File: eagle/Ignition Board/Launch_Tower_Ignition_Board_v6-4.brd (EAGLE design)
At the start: 87.6 x 69.8 mm, 41 parts, among them IC1 INVERT GATES, IC2 OPTOISOLATOR, Q1 NMOSFET, U1 SN65220DBV

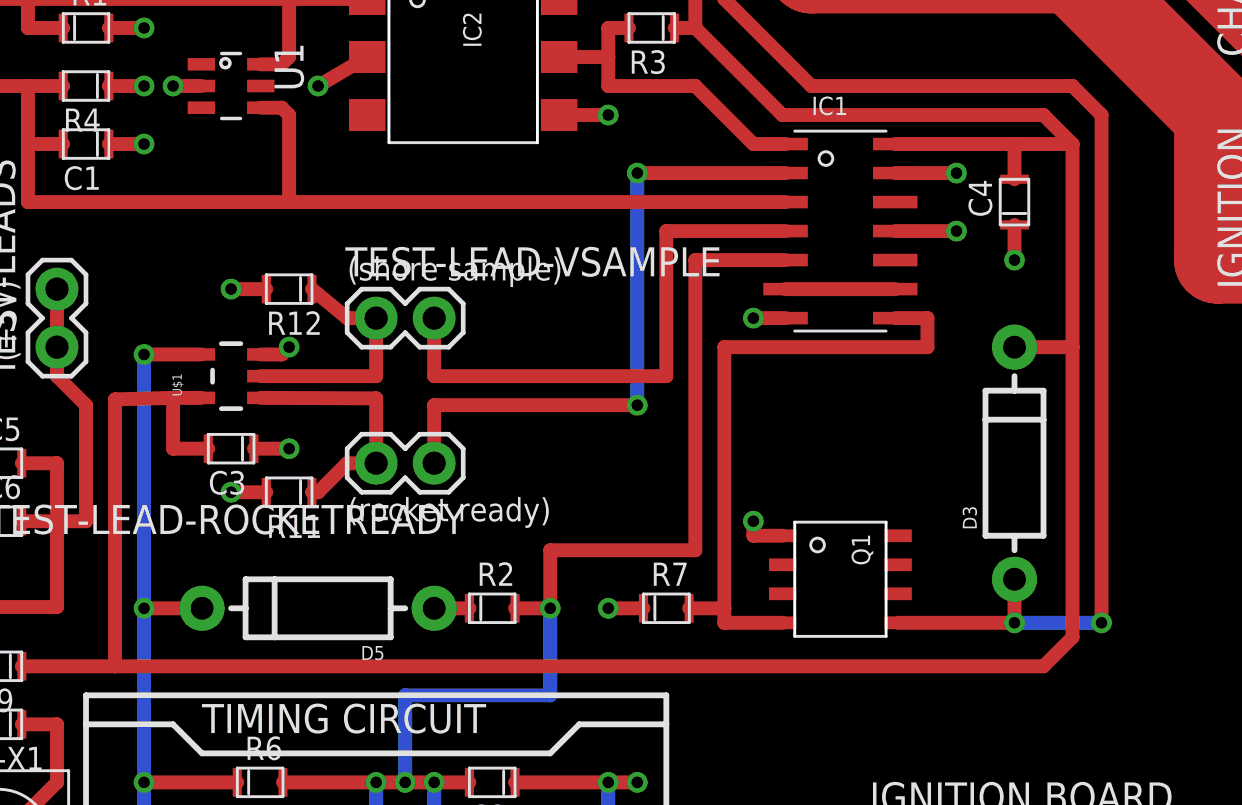
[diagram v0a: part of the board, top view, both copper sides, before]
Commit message: Minor changes to Ignition board and library - smaller diode Signed-off-by: richard <richard@mailwh.com>
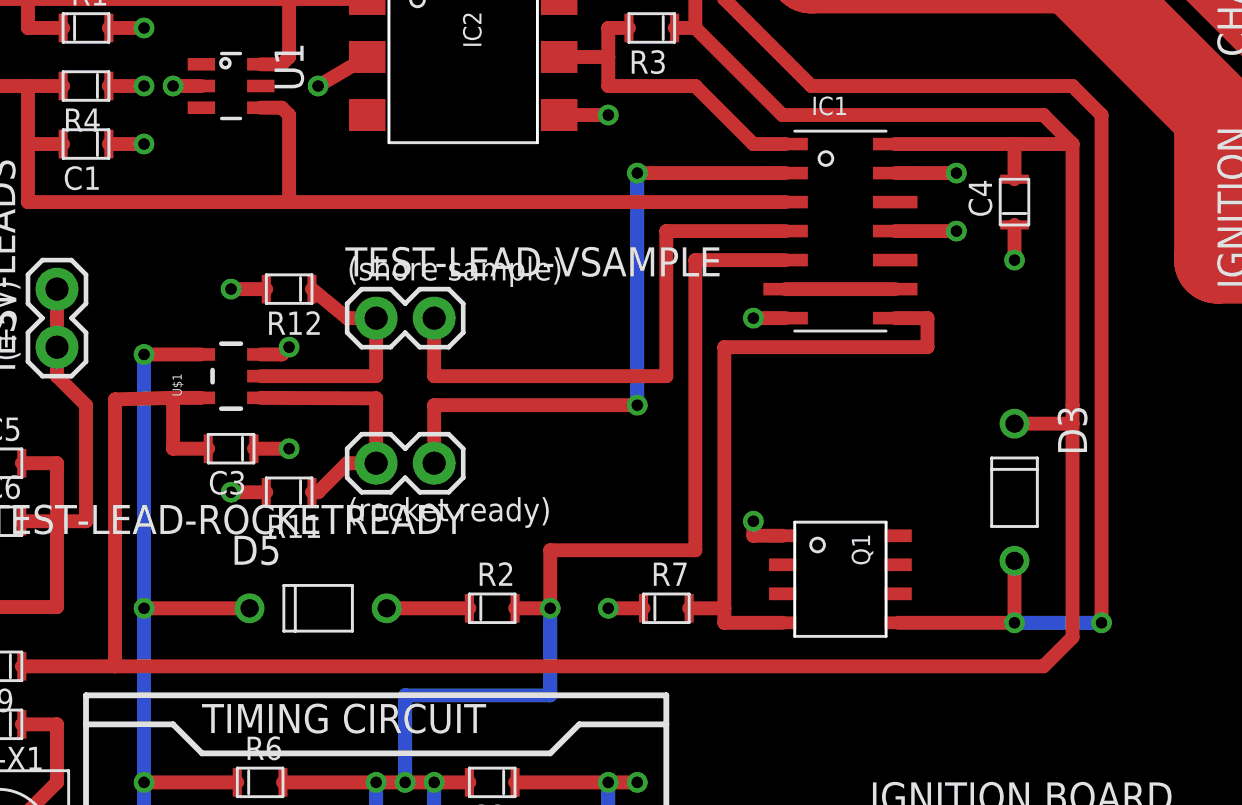
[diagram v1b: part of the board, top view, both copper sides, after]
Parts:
- D3, D5: value (none) -> DIODE-NORM; device SparkFun:DIODE-1N4001 -> launch-tower:DIODE
- moved D3 1.27 mm to (61.0, 20.3), turned to 270 degrees
- turned D5 to 0 degrees
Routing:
- net N$8: track 1.54 -> 3.62 mm
- net N$13: track 31.7 -> 33.7 mm
- net N$9: track 62.2 -> 63.0 mm
- net VDD: track 148.7 -> 149.5 mm
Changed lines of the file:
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@@
 <element name="JP2" library="launch-tower" package="SCREW-TERM-5MM" value="" x="7.62" y="17.78" rot="R270"/>
 <element name="JP3" library="launch-tower" package="SCREW-TERM-5MM" value="" x="7.62" y="39.37" rot="R270"/>
-<element name="D5" library="SparkFun" package="DIODE-1N4001" value="" x="30.48" y="15.24" rot="R180"/>
-<element name="D3" library="SparkFun" package="DIODE-1N4001" value="" x="60.96" y="21.59" rot="R90"/>
+<element name="D5" library="launch-tower" package="DIODE" value="DIODE-NORM" x="30.48" y="15.24"/>
+<element name="D3" library="launch-tower" package="DIODE" value="DIODE-NORM" x="60.96" y="20.32" rot="R270"/>
 <element name="U$2" library="mount" package="#4/.300-BARE+STD_NUT_OR_STAR_WASHER" value="#4-BARE_MOUNTING_HOLE/.300" x="5.08" y="64.77"/>
 <element name="U$3" library="mount" package="#4/.300-BARE+STD_NUT_OR_STAR_WASHER" value="#4-BARE_MOUNTING_HOLE/.300" x="82.55" y="64.77"/>
@@
 <contactref element="D3" pad="A"/>
 <wire x1="55.867" y1="14.605" x2="60.96" y2="14.605" width="0.6096" layer="1"/>
-<wire x1="60.96" y1="14.605" x2="60.96" y2="16.51" width="0.6096" layer="1"/>
+<wire x1="60.96" y1="14.605" x2="60.96" y2="17.32" width="0.6096" layer="1"/>
 <wire x1="64.77" y1="14.605" x2="60.96" y2="14.605" width="0.6096" layer="16"/>
 <via x="64.77" y="14.605" extent="1-16" drill="0.508"/>
@@
 <signal name="VDD">
 <contactref element="D3" pad="C"/>
-<wire x1="63.5" y1="35.56" x2="63.5" y2="26.67" width="0.6096" layer="1"/>
-<wire x1="63.5" y1="26.67" x2="63.5" y2="13.97" width="0.6096" layer="1"/>
+<wire x1="63.5" y1="35.56" x2="63.5" y2="24.13" width="0.6096" layer="1"/>
+<wire x1="63.5" y1="24.13" x2="63.5" y2="13.97" width="0.6096" layer="1"/>
 <wire x1="63.5" y1="13.97" x2="62.23" y2="12.7" width="0.6096" layer="1"/>
-<wire x1="63.5" y1="26.67" x2="60.96" y2="26.67" width="0.6096" layer="1"/>
 <wire x1="21.59" y1="12.7" x2="21.59" y2="24.384" width="0.6096" layer="1"/>
 <contactref element="U$1" pad="5"/>
@@
 <wire x1="24.13" y1="22.225" x2="25.67" y2="22.225" width="0.6096" layer="1"/>
 <wire x1="60.96" y1="34.02" x2="60.96" y2="35.56" width="0.6096" layer="1"/>
+<wire x1="60.96" y1="23.32" x2="63.5" y2="23.32" width="0.6096" layer="1"/>
+<wire x1="63.5" y1="23.32" x2="63.5" y2="24.13" width="0.254" layer="1"/>
 </signal>
 <signal name="N$4">
@@
 <contactref element="U$1" pad="4"/>
 <contactref element="D5" pad="C"/>
-<wire x1="25.4" y1="15.24" x2="22.86" y2="15.24" width="0.6096" layer="1"/>
+<wire x1="27.48" y1="15.24" x2="22.86" y2="15.24" width="0.6096" layer="1"/>
 <wire x1="22.86" y1="7.62" x2="22.86" y2="15.24" width="0.6096" layer="16"/>
 <via x="22.86" y="7.62" extent="1-16" drill="0.508"/>
@@
 <contactref element="D5" pad="A"/>
 <contactref element="R2" pad="CATHODE"/>
-<wire x1="37.1" y1="15.24" x2="35.56" y2="15.24" width="0.6096" layer="1"/>
+<wire x1="37.1" y1="15.24" x2="33.48" y2="15.24" width="0.6096" layer="1"/>
 </signal>
 </signals>

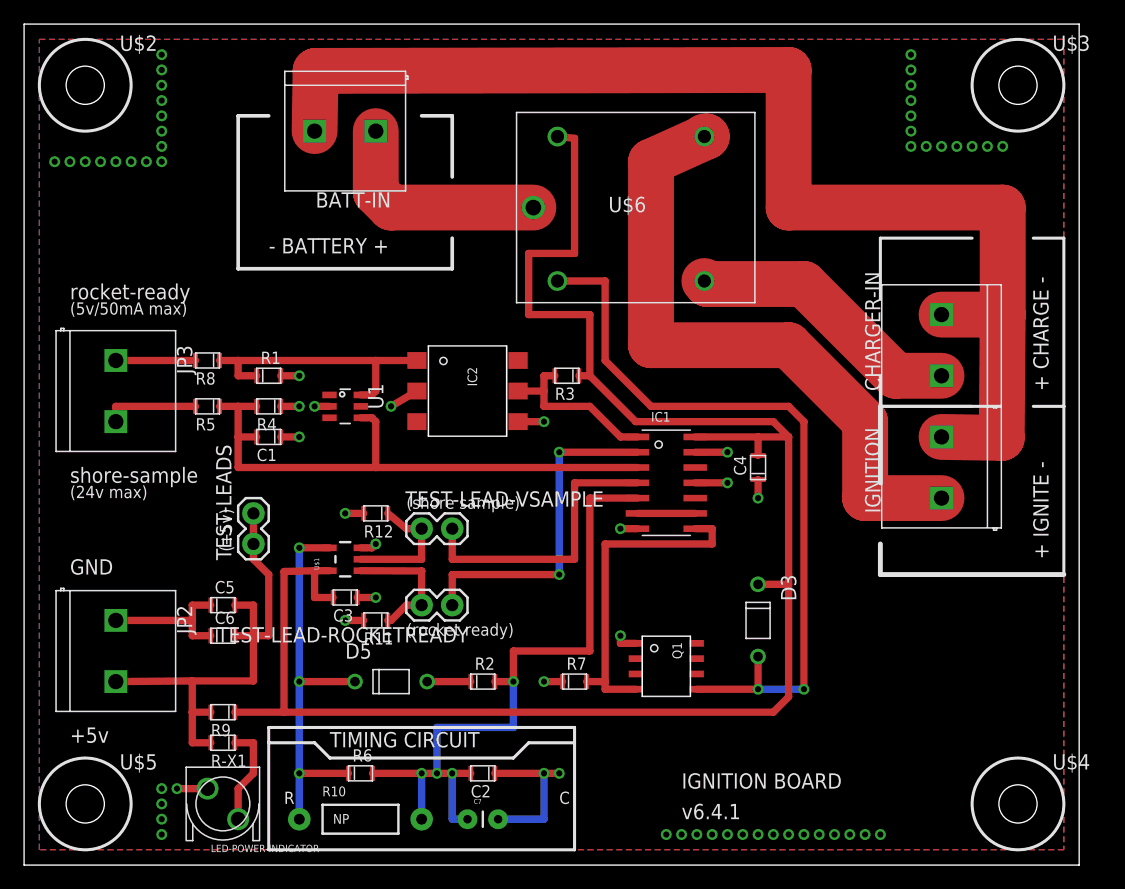
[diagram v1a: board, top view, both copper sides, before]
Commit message: Cleaned up ignition board for manufacturing - ERCs, DRCs, flood fills, switched MOSFET to have a higher Vgs on, added LED for the ignition on circuit, cleaned up tsilk layer.
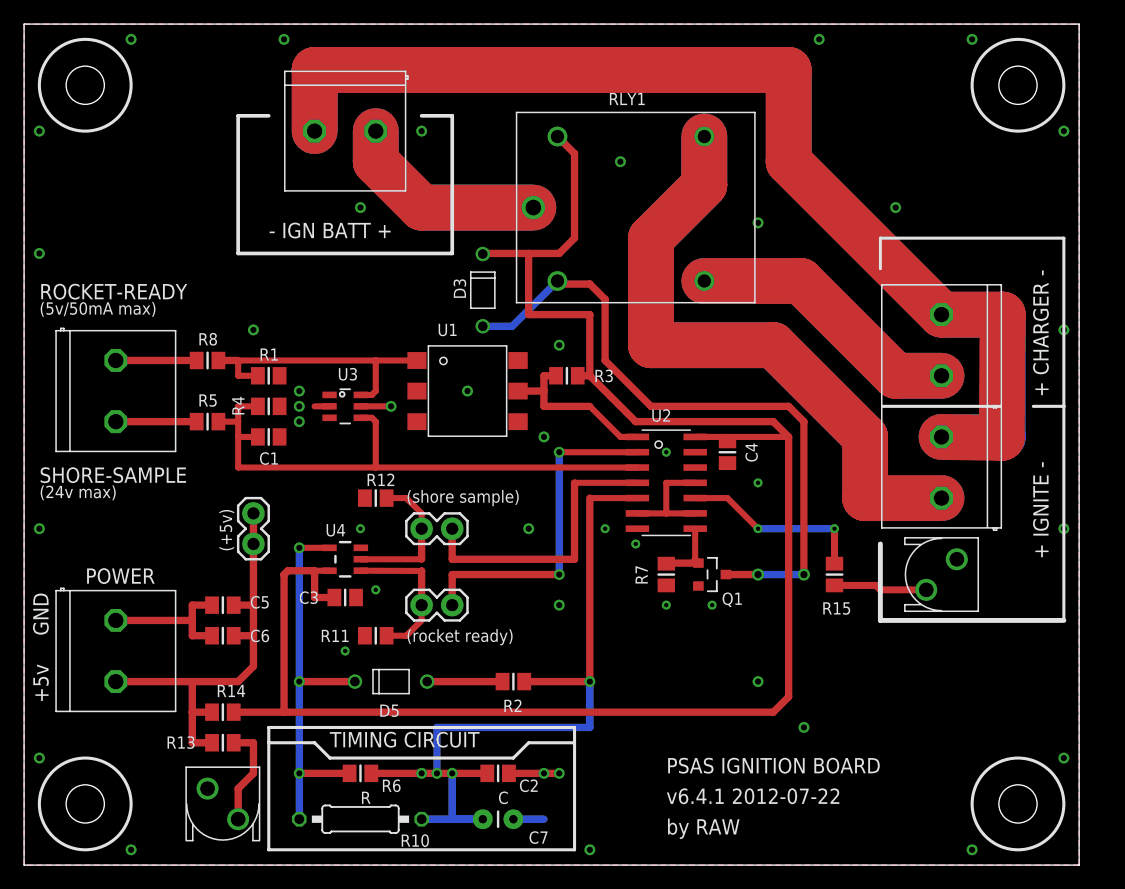
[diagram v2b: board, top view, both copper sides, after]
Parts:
- removed IC2: OPTOISOLATOR, launch-tower:4N35-300E
- removed R-X1: 560, launch-tower:0805
- removed R9: 0, launch-tower:0805
- added LED-POWER-INDICATOR1: LED-550-XX04, launch-tower:LED-550
- added R13, R15: 560, rcl_custom:0805-B
- added R14: 0, rcl_custom:0805-B
- added U3: SN65220DBV, sn65220:SOT23-6L
- C1, C2, C3, C4, C5, C6, R1, R11, R12, R2, R3, R6, R7, R8: device launch-tower:0805 -> rcl_custom:0805-B
- Q1: value NMOSFET -> PMV45EN; device launch-tower:FETSO-8 -> Tova:SOT23
- R10: device SparkFun:AXIAL-0.4 -> rcl_custom:0207/10
- R4: value 10k -> 2.6k; device launch-tower:0805 -> rcl_custom:0805-B
- R5: value 2.6k -> 10k; device launch-tower:0805 -> rcl_custom:0805-B
- U1: value SN65220DBV -> OPTOISOLATOR; device sn65220:SOT23-6L -> launch-tower:4N35-300E
- moved D3 35.7 mm to (38.1, 47.8)
- moved R7 11.7 mm to (53.3, 24.1), turned to 270 degrees
- moved U1 10.2 mm to (36.8, 39.4)
- moved Q1 8.52 mm to (57.1, 24.1)
- moved C4 2.84 mm to (58.4, 34.3)
- moved R2 2.54 mm to (40.6, 15.2)
- moved C7 1.27 mm to (38.1, 3.81)
- moved R5 1.27 mm to (15.2, 36.8)
- moved R11 1.27 mm to (29.2, 19.1)
- moved R12 1.27 mm to (29.2, 30.5)
- moved C2 1.27 mm to (39.4, 7.62)
- renumbered IC1 to U2, TEST-LEADS to FOR-TESTING, U$1 to U4, U$6 to RLY1
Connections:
- removed net GND: C1.CATHODE, C2.CATHODE, C3.CATHODE, C4.CATHODE, C5.CATHODE, C6.CATHODE, C7.2, IC2.2, IC2.4, JP2.1, LED-POWER-INDICATOR.CATHODE, Q1.1, R1.ANODE, R11.ANODE, R12.ANODE, R4.CATHODE, R7.CATHODE, U1.2, U1.5, U2.11, U2.13, U2.7, U4.3
- new net N$14: R15.1, U2.10
- new net N$18: LED-POWER-INDICATOR1.ANODE, R15.2
- new net NAME: C1.2, C2.2, C3.2, C4.2, C5.2, C6.2, C7.2, JP2.1, LED-POWER-INDICATOR.CATHODE, LED-POWER-INDICATOR1.CATHODE, Q1.2, R1.1, R11.1, R12.1, R4.2, R7.2, U1.2, U1.4, U2.13, U2.7, U3.2, U3.5, U4.3
- net N$1: now also R12.2; no longer R12.CATHODE
- net N$10: now also Q1.1, R7.1; no longer Q1.4, R7.ANODE
- net N$12: now also C5.1, C6.1, R13.1, R14.1; no longer C5.ANODE, C6.ANODE, R-X1.ANODE, R9.ANODE
- net N$13: now also R10.1, R6.2; no longer R10.P$1, R6.CATHODE
- net N$15: now also C2.1, R10.2, R2.1, R6.1; no longer C2.ANODE, R10.P$2, R2.ANODE, R6.ANODE
- net N$2: now also R13.2; no longer R-X1.CATHODE
- net N$3: now also R3.1, U1.5; no longer IC2.5, R3.ANODE
- net N$4: now also R8.1; no longer R8.ANODE
- net N$5: now also R11.2; no longer R11.CATHODE
- net N$7: now also C1.1, R4.1, R5.2, U3.4; no longer C1.ANODE, R4.ANODE, R5.CATHODE, U1.4
- net N$8: now also R2.2; no longer R2.CATHODE
- net N$9: now also Q1.3; no longer Q1.5
- net N-NOT2: now also U2.11
- net ROCKET-READY: now also R1.2, R8.2, U1.1, U3.6; no longer IC2.1, R1.CATHODE, R8.CATHODE, U1.6
- net VDD: now also C3.1, C4.1, R14.2, R3.2; no longer C3.ANODE, C4.ANODE, R3.CATHODE, R9.CATHODE
- net VSAMPLE: now also R5.1; no longer R5.ANODE
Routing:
- net GND-BATT: track 102.7 -> 180.7 mm
- net GND: track 55.7 -> 0.00 mm, vias 66 -> 0
- net VCC-IGNITION: track 53.6 -> 103.1 mm
- net BATT-CHARG-RELAY: track 23.0 -> 45.9 mm
- net NAME: track 0.00 -> 22.6 mm, vias 0 -> 43
- net N$10: track 27.7 -> 5.66 mm
- net VCC-BATT: track 18.7 -> 34.4 mm
- net N$14: track 0.00 -> 15.5 mm, vias 0 -> 2
- net N$15: track 58.1 -> 66.0 mm
- net N$9: track 63.0 -> 55.2 mm
- net N$18: track 0.00 -> 7.77 mm
- net N-NOT2: track 4.80 -> 9.74 mm
- net N$12: track 41.0 -> 36.3 mm
- net N$8: track 3.62 -> 6.26 mm
- net N$1: track 10.9 -> 12.3 mm
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- added copper zone on layer 1, net NAME
- added copper zone on layer 16, net NAME
- removed copper zone on layer 1, net GND
- removed copper zone on layer 16, net GND
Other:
- board text added: "+ CHARGER -"
- board text added: "- IGN BATT +"
- board text added: "POWER"
- board text added: "PSAS IGNITION BOARD"
- board text added: "ROCKET-READY"
- board text added: "SHORE-SAMPLE"
- board text added: "by RAW"
- board text added: "v6.4.1 2012-07-22"
- board text removed: "+ CHARGE -"
- board text removed: "- BATTERY +"
- board text removed: "IGNITION BOARD"
- board text removed: "rocket-ready"
- board text removed: "shore-sample"
- board text removed: "v6.4.1"

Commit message: Updated Eagle File
Modified ignition board resistor R8
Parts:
- D5: value DIODE-NORM -> (none)
- R8: value 350 -> 100
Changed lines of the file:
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@@
 <?xml version="1.0" encoding="utf-8"?>
 <!DOCTYPE eagle SYSTEM "eagle.dtd">
-<eagle version="6.2">
+<eagle version="6.4">
 <drawing>
 <settings>
@@
 <setting verticaltext="up"/>
 </settings>
-<grid distance="0.01" unitdist="inch" unit="inch" style="lines" multiple="1" display="yes" altdistance="0.005" altunitdist="inch" altunit="inch"/>
+<grid distance="0.05" unitdist="inch" unit="inch" style="lines" multiple="1" display="yes" altdistance="0.005" altunitdist="inch" altunit="inch"/>
 <layers>
 <layer number="1" name="Top" color="4" fill="1" visible="yes" active="yes"/>
@@
 <layer number="14" name="Route14" color="1" fill="6" visible="no" active="no"/>
 <layer number="15" name="Route15" color="4" fill="6" visible="no" active="no"/>
-<layer number="16" name="Bottom" color="1" fill="1" visible="no" active="yes"/>
+<layer number="16" name="Bottom" color="1" fill="1" visible="yes" active="yes"/>
 <layer number="17" name="Pads" color="2" fill="1" visible="yes" active="yes"/>
 <layer number="18" name="Vias" color="2" fill="1" visible="yes" active="yes"/>
@@
 <layer number="20" name="Dimension" color="15" fill="1" visible="yes" active="yes"/>
 <layer number="21" name="tPlace" color="16" fill="1" visible="yes" active="yes"/>
-<layer number="22" name="bPlace" color="14" fill="1" visible="no" active="yes"/>
+<layer number="22" name="bPlace" color="14" fill="1" visible="yes" active="yes"/>
 <layer number="23" name="tOrigins" color="15" fill="1" visible="yes" active="yes"/>
-<layer number="24" name="bOrigins" color="15" fill="1" visible="no" active="yes"/>
-<layer number="25" name="tNames" color="7" fill="1" visible="yes" active="yes"/>
+<layer number="24" name="bOrigins" color="15" fill="1" visible="yes" active="yes"/>
+<layer number="25" name="tNames" color="7" fill="1" visible="no" active="yes"/>
 <layer number="26" name="bNames" color="7" fill="1" visible="no" active="yes"/>
 <layer number="27" name="tValues" color="7" fill="1" visible="no" active="yes"/>
@@
 <layer number="43" name="vRestrict" color="2" fill="10" visible="no" active="yes"/>
 <layer number="44" name="Drills" color="7" fill="1" visible="no" active="yes"/>
-<layer number="45" name="Holes" color="7" fill="1" visible="no" active="yes"/>
+<layer number="45" name="Holes" color="7" fill="1" visible="yes" active="yes"/>
 <layer number="46" name="Milling" color="3" fill="1" visible="no" active="yes"/>
 <layer number="47" name="Measures" color="7" fill="1" visible="no" active="yes"/>
-<layer number="48" name="Document" color="7" fill="1" visible="yes" active="yes"/>
-<layer number="49" name="Reference" color="7" fill="1" visible="yes" active="yes"/>
+<layer number="48" name="Document" color="7" fill="1" visible="no" active="yes"/>
+<layer number="49" name="Reference" color="7" fill="1" visible="no" active="yes"/>
 <layer number="50" name="dxf" color="7" fill="1" visible="no" active="no"/>
-<layer number="51" name="tDocu" color="6" fill="1" visible="no" active="yes"/>
+<layer number="51" name="tDocu" color="6" fill="1" visible="yes" active="yes"/>
 <layer number="52" name="bDocu" color="7" fill="1" visible="no" active="yes"/>
 <layer number="53" name="tGND_GNDA" color="7" fill="9" visible="no" active="no"/>
@@
 </class>
 </classes>
-<designrules>
+<designrules name="default">
 <description language="en">&lt;b&gt;EAGLE Design Rules&lt;/b&gt;
 &lt;p&gt;
@@
 <attribute name="VALUE" x="8.89" y="43.18" size="1.27" layer="27" rot="R270"/>
 </element>
-<element name="D5" library="launch-tower" package="DIODE" value="DIODE-NORM" x="30.48" y="15.24" smashed="yes">
+<element name="D5" library="launch-tower" package="DIODE" value="" x="30.48" y="15.24" smashed="yes">
 <attribute name="NAME" x="29.464" y="12.319" size="1.016" layer="25" ratio="10"/>
 <attribute name="VALUE" x="26.67" y="12.065" size="1.27" layer="27"/>
@@
 </element>
 <element name="LED-POWER-INDICATOR" library="launch-tower" package="LED-550" value="LED-550-XX04" x="16.51" y="5.08" smashed="yes"/>
-<element name="R8" library="rcl_custom" package="0805-B" value="350" x="15.24" y="41.91" smashed="yes">
+<element name="R8" library="rcl_custom" package="0805-B" value="100" x="15.24" y="41.91" smashed="yes">
 <attribute name="NAME" x="14.44" y="43.164" size="1.016" layer="25" ratio="10"/>
 <attribute name="VALUE" x="14.44" y="39.91" size="1" layer="27" ratio="10"/>
@@
 </signal>
 </signals>
-<errors>
-</errors>
 </board>
 </drawing>
